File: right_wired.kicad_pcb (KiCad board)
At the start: 2 copper layers, 148.2 x 107.5 mm, 49 parts

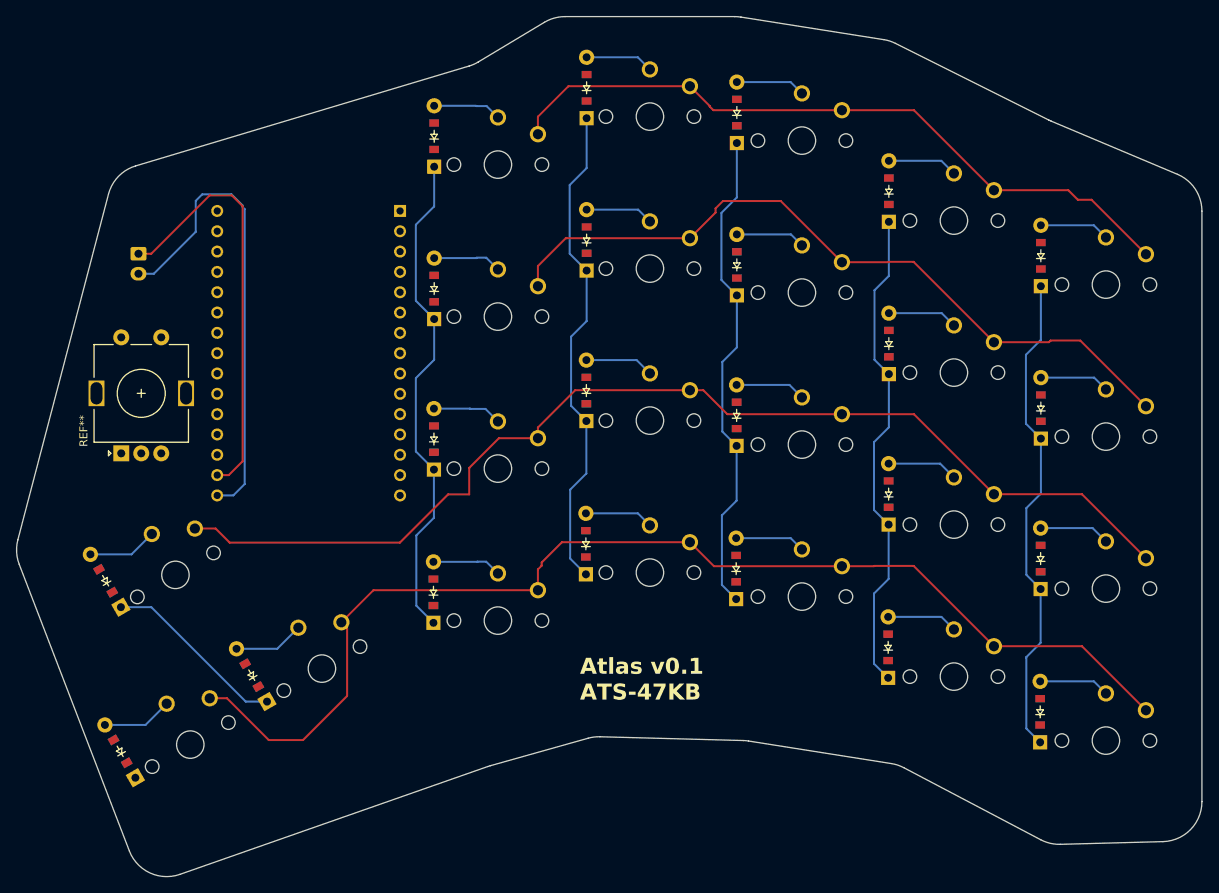
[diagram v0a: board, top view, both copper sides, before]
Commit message: Wired pcbs for row/column scanning
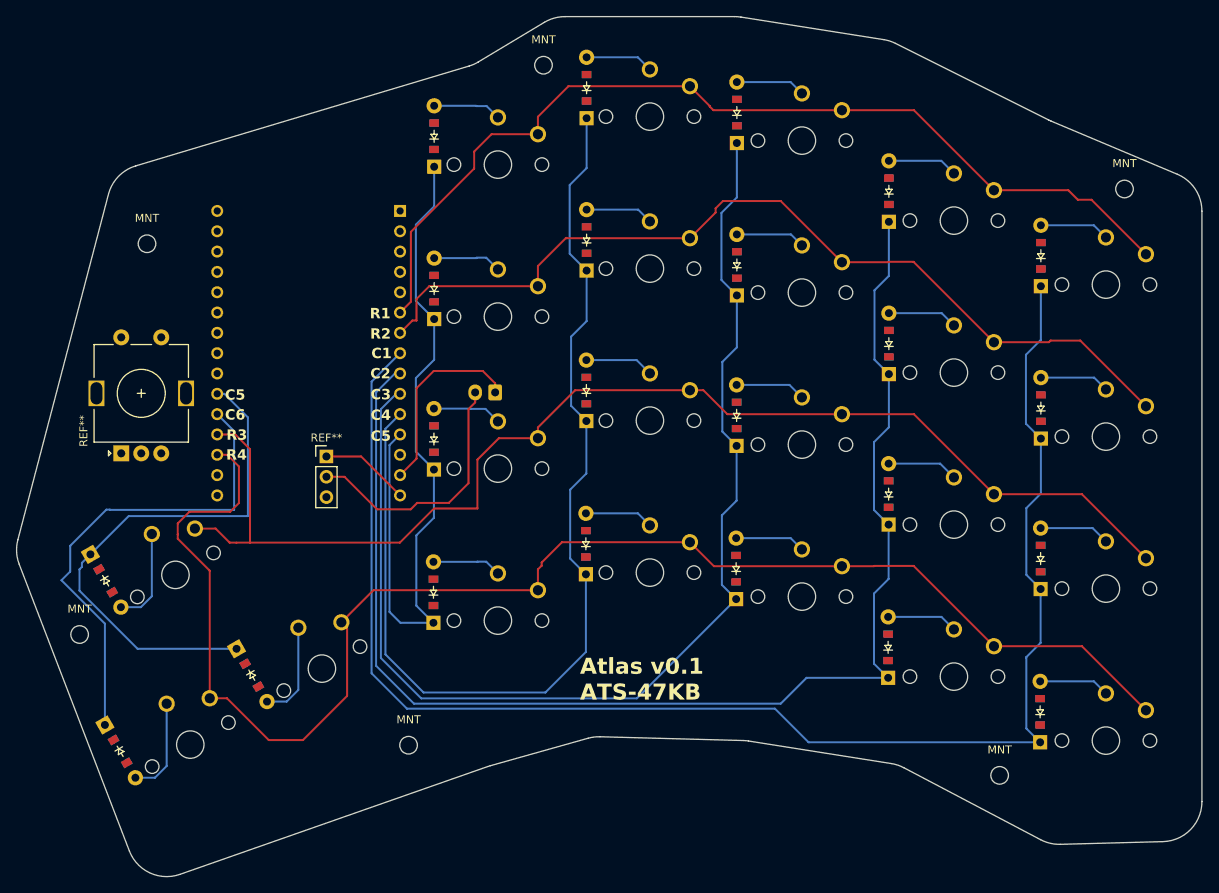
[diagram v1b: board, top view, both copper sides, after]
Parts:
- added MNT: MountingHole_2.2mm_M2, MountingHole:MountingHole_2.2mm_M2, F.Cu at (286.7, 4.35)
- added MNT: MountingHole_2.2mm_M2, MountingHole:MountingHole_2.2mm_M2, F.Cu at (212.8, 0.58)
- added MNT: MountingHole_2.2mm_M2, MountingHole:MountingHole_2.2mm_M2, F.Cu at (302.3, -68.9)
- added MNT: MountingHole_2.2mm_M2, MountingHole:MountingHole_2.2mm_M2, F.Cu at (229.7, -84.4)
- added MNT: MountingHole_2.2mm_M2, MountingHole:MountingHole_2.2mm_M2, F.Cu at (171.7, -13.3)
- added MNT: MountingHole_2.2mm_M2, MountingHole:MountingHole_2.2mm_M2, F.Cu at (180.1, -62.1)
- added REF**: PinHeader_1x03_P2.54mm_Vertical, Connector_PinHeader_2.54mm:PinHeader_1x03_P2.54mm_Vertical, F.Cu at (202.6, -35.5)
- moved BAT 47.8 mm to (223.7, -43.5), turned to 180 degrees
- turned D21 to -60 degrees
- turned D22 to -60 degrees
- turned D23 to -60 degrees
- renumbered REF** to BAT
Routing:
- net (no net): track 910.5 -> 1501.9 mm
- net mirror_ring_bottom: track 8.73 -> 12.2 mm
- net mirror_pinky_bottom: track 8.82 -> 12.3 mm
- net mirror_macro_bottom: track 8.82 -> 12.3 mm
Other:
- board text added: "C5"
- board text added: "C6"
- board text added: "R1"
- board text added: "R2"
- board text added: "R3"
- board text added: "R4"
- board text added: "С1"
- board text added: "С2"
- board text added: "С3"
- board text added: "С4"
- board text added: "С5"

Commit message: Updated diod placement
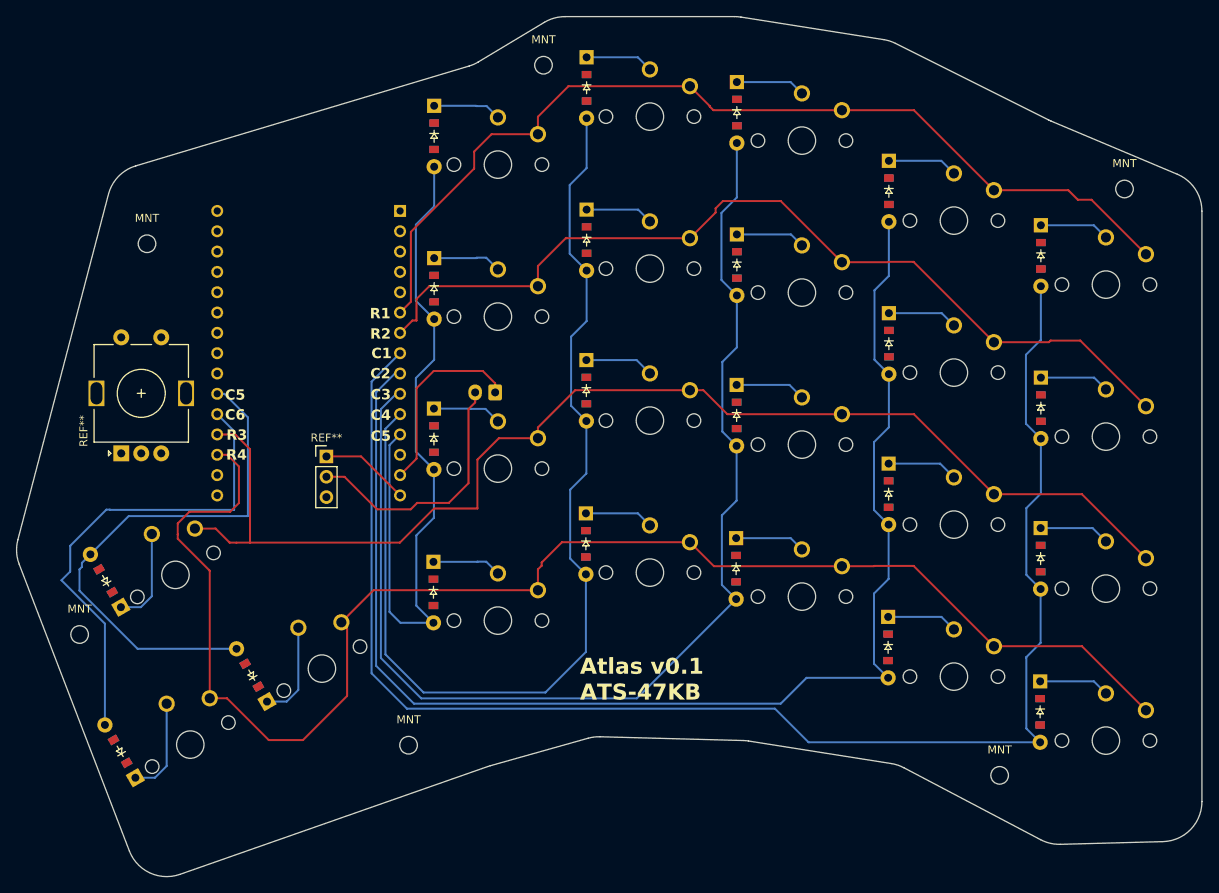
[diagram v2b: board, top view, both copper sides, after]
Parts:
- turned D17 to -90 degrees (x5)
- turned D18 to -90 degrees (x5)
- turned D19 to -90 degrees (x5)
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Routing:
- net (no net): track 1501.9 -> 1441.6 mm
- net mirror_pinky_bottom: track 12.3 -> 72.6 mm
